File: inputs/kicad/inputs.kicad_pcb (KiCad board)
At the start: 2 copper layers, 93.3 x 31.7 mm, 33 parts, among them P1 MOLEX-0431603103, P2 MOLEX-0431603103, P3 TE-282836-4, P4 TE-282836-4, P5 TE-282836-4, P6 TE-282836-4, P7 CONN_01X05, U1 PIC16F1829LIN

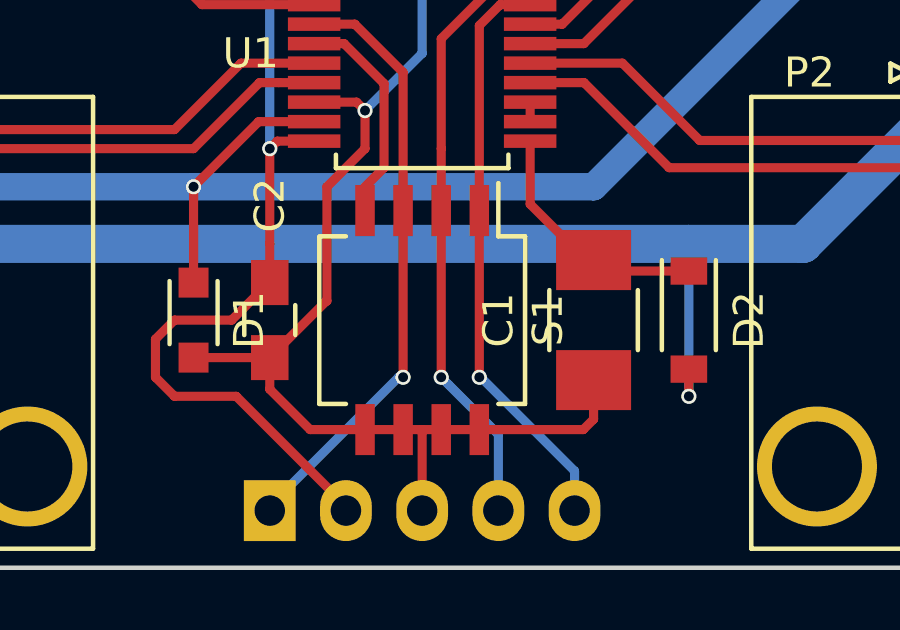
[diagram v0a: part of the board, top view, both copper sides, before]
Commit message: [inputs] Updating to use standard libraries
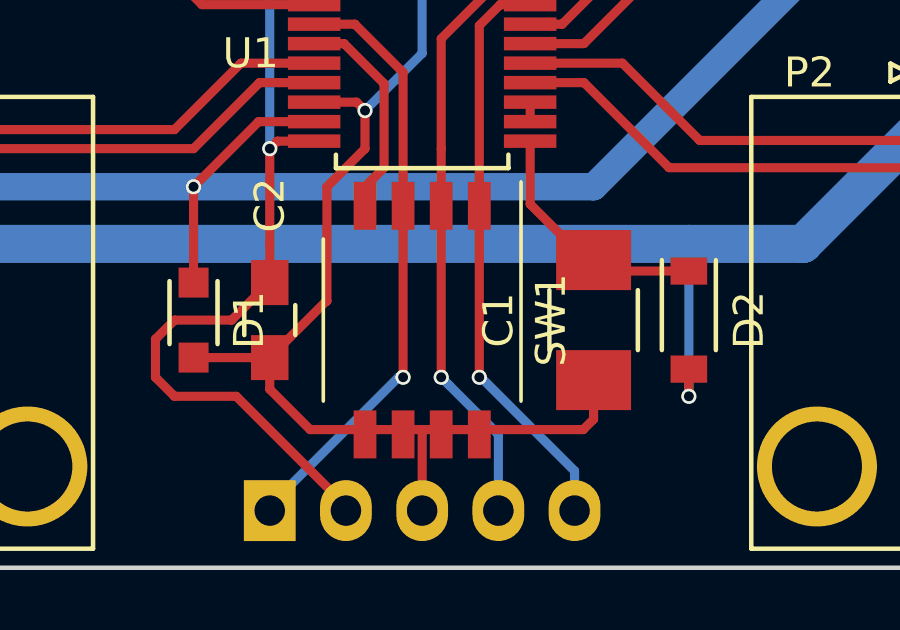
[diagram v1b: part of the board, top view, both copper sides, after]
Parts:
- removed S1: DIP_SWITCH_4, footprints:Copal_CHS-04TB
- added SW1: SW_DIP_x04, Buttons_Switches_SMD:SW_DIP_x4_W7.62mm_Slide_Copal_CHS-B, F.Cu at (194.9, 79.4)
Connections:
- net /Sheet584D6B96/CHAN_A renamed /IN0
- net /Sheet584D6B96/CHAN_B renamed /IN1
- net /Sheet584D7AB5/CHAN_A renamed /IN4
- net /Sheet584D7AB5/CHAN_B renamed /IN5
- net /Sheet584D8209/CHAN_A renamed /IN2
- net /Sheet584D8209/CHAN_B renamed /IN3
- net /Sheet584D84B8/CHAN_A renamed /IN6
- net /Sheet584D84B8/CHAN_B renamed /IN7

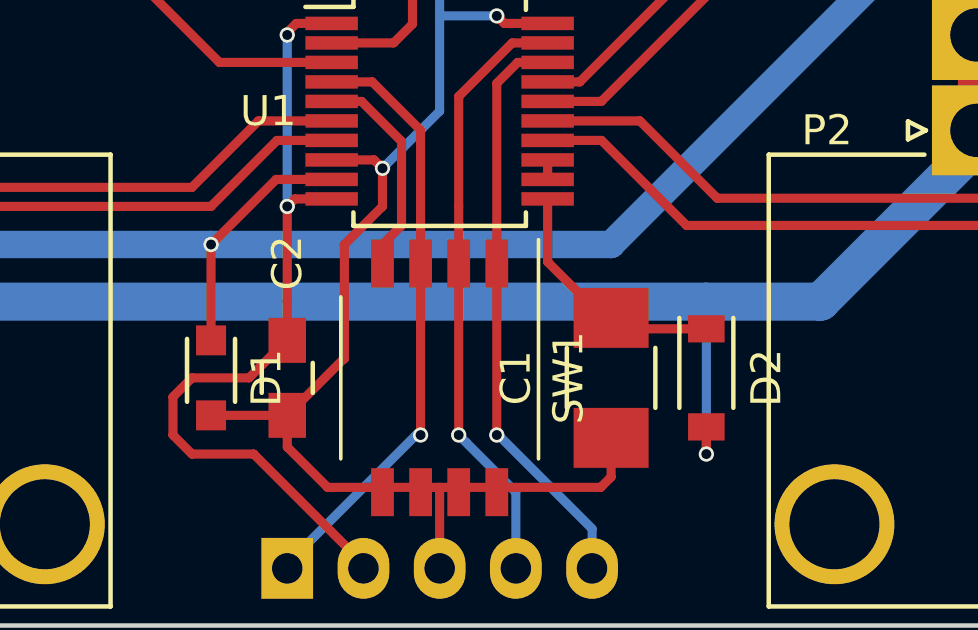
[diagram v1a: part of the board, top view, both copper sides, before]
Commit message: First working NRF52 master with two slave PIC nodes
# Software

* Using LIN 2.x checksum instead of LIN 1.x
* Using 19200 baudrate instead of 20000 for compatibility with NRF52
* Setting only the NRF52 as master
* Deactivating sleep mode for PIC as it was broken
* Ignoring break signal (not generated by NRF52 yet)
* Code cleaning: removing unused functions

# Boards

* Updating Git submodules
* Moving text references for the 8x input board
* Adding a TODO note for replacing the LIN pull-up resistor
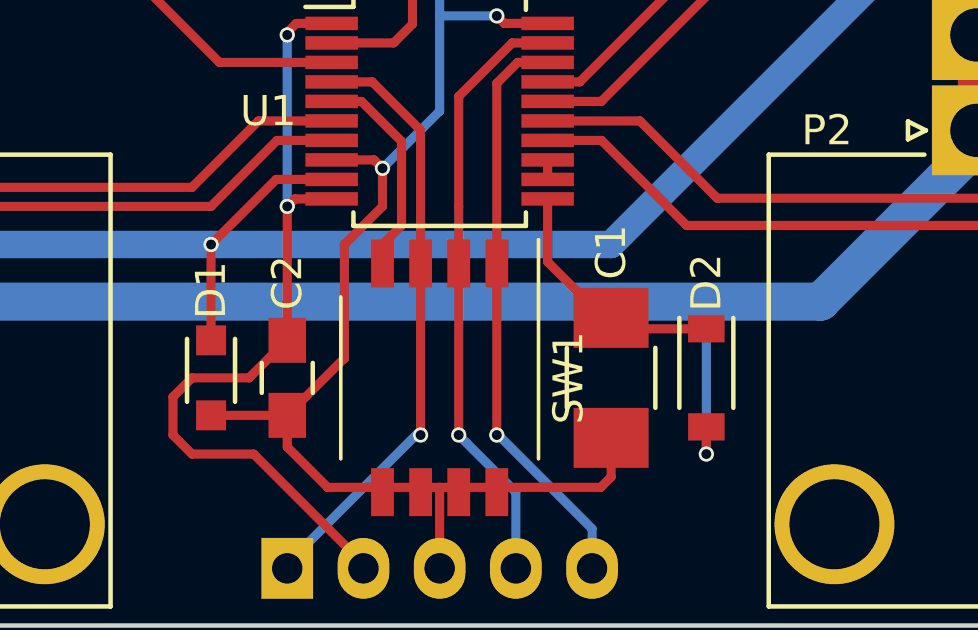
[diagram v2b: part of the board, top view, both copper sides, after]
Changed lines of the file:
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@@
-(kicad_pcb (version 4) (host pcbnew 4.0.4+e1-6308~48~ubuntu16.04.1-stable)
+(kicad_pcb (version 4) (host pcbnew 4.0.5-e0-6337~49~ubuntu16.04.1)
   (general
     (links 75)
@@
     (tags "capacitor 1210")
     (attr smd)
-    (fp_text reference C1 (at 0 3.175 270) (layer F.SilkS)
+    (fp_text reference C1 (at -4.191 0 270) (layer F.SilkS)
       (effects (font (size 1 1) (thickness 0.15)))
     )
@@
     (tags "capacitor 0805")
     (attr smd)
-    (fp_text reference C2 (at -3.83 0 270) (layer F.SilkS)
+    (fp_text reference C2 (at -3.175 0 270) (layer F.SilkS)
       (effects (font (size 1 1) (thickness 0.15)))
     )
@@
     (tags SOD-323)
     (attr smd)
-    (fp_text reference D1 (at 0 -1.85 270) (layer F.SilkS)
+    (fp_text reference D1 (at -2.921 0 270) (layer F.SilkS)
       (effects (font (size 1 1) (thickness 0.15)))
     )
@@
     (tags SOD-123)
     (attr smd)
-    (fp_text reference D2 (at 0 -2 270) (layer F.SilkS)
-      (effects (font (size 1 1) (thickness 0.15)))
-    )
+    (fp_text reference D2 (at -3.175 0 270) (layer F.SilkS)
+      (effects (font (size 1 1) (thickness 0.15)))
+    )
